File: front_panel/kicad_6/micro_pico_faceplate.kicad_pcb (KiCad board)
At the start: 2 copper layers, 137.2 x 114.3 mm, 36 parts

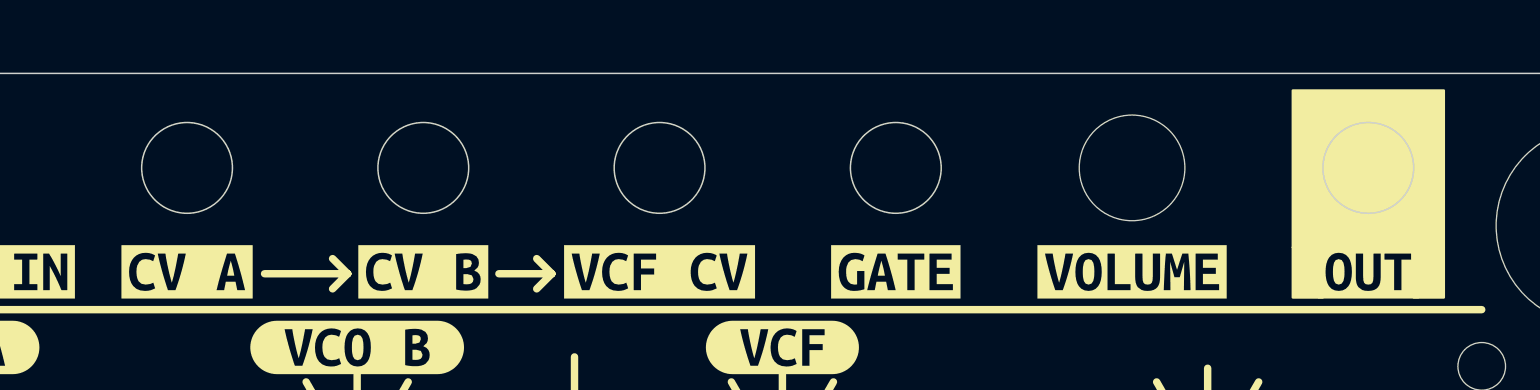
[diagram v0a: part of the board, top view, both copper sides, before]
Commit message: Add mod-wheel VCA, fix occasional VCO freq locking
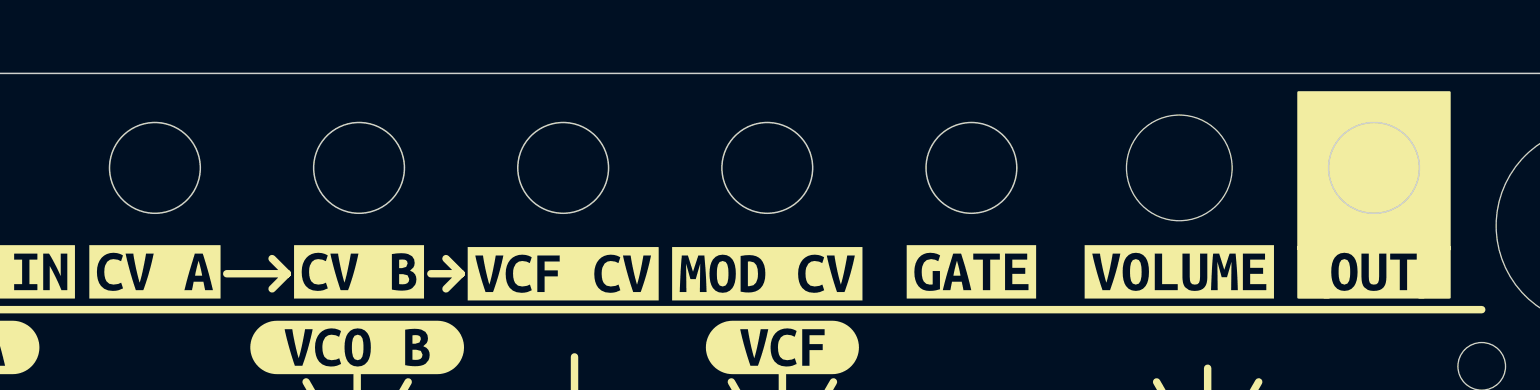
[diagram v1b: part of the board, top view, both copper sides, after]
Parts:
- added kibuzzard-63408637: G***, kibuzzard-63408637, F.Cu at (140.0, 42.7)
- moved kibuzzard-62EED338 6.48 mm to (126.2, 42.7)
- moved kibuzzard-62EED341 5.08 mm to (153.7, 42.5)
- moved kibuzzard-62EED326 4.32 mm to (112.5, 42.5)
- moved kibuzzard-62EED34B 3.17 mm to (167.6, 42.5)
- moved kibuzzard-62EED31D 2.16 mm to (98.8, 42.5)
- moved kibuzzard-62EED355 0.38 mm to (180.7, 42.5)
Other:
- outline, holes or cut-outs redrawn
